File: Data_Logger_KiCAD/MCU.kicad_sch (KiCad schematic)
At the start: 40 parts, among them J1 USB_C_Receptacle_USB2.0_16P, J2 Screw_Terminal_01x02, Q1 Q_NMOS_GSD, SW1 SW_Push, SW2 SW_Push, U2 ESP32-S3, Y2 Crystal, Y3 Crystal_GND24

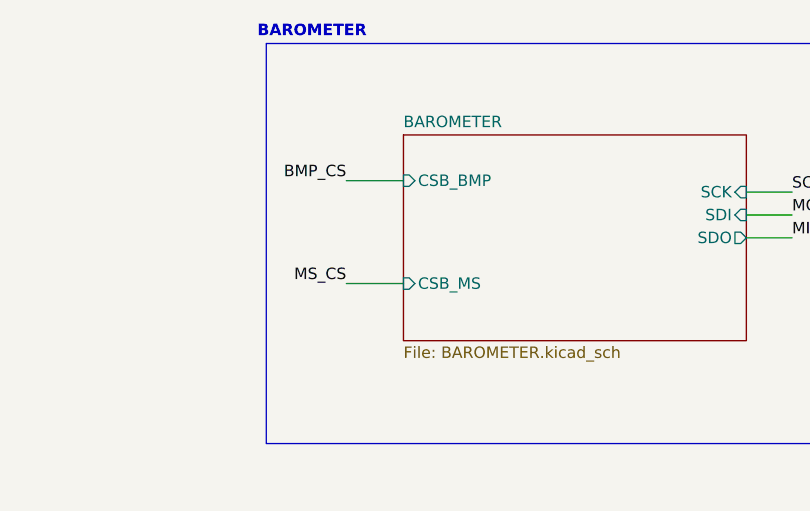
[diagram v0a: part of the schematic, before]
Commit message: synced sheet pins in Data_Logger_Board_pro
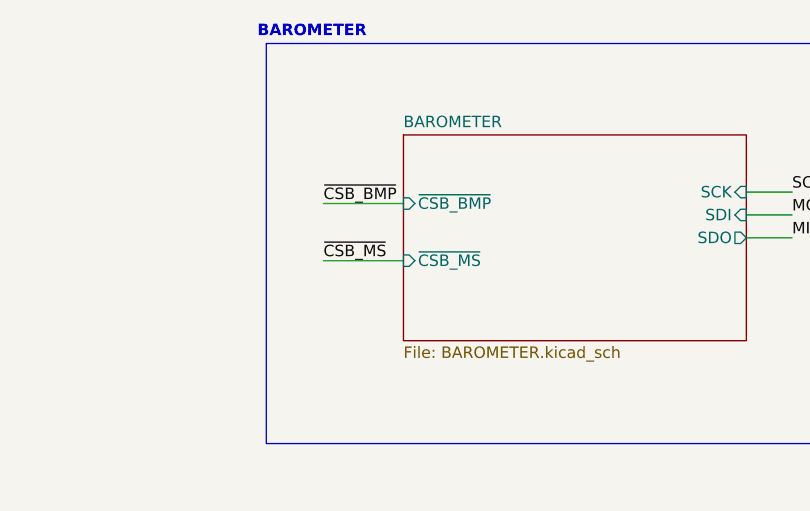
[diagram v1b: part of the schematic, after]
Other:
- sheet BAROMETER ports: added ~{CSB_BMP}, ~{CSB_MS}; removed CSB_BMP, CSB_MS
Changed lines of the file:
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@@
 	(wire
 		(pts
-			(xy 396.24 80.01) (xy 402.59 80.01)
+			(xy 269.24 80.01) (xy 275.59 80.01)
 		)
 		(stroke
@@
 	(wire
 		(pts
-			(xy 269.24 80.01) (xy 275.59 80.01)
+			(xy 185.42 133.35) (xy 193.04 133.35)
 		)
 		(stroke
@@
 	(wire
 		(pts
-			(xy 185.42 133.35) (xy 193.04 133.35)
+			(xy 59.69 87.63) (xy 59.69 85.09)
 		)
 		(stroke
@@
 	(wire
 		(pts
-			(xy 59.69 87.63) (xy 59.69 85.09)
+			(xy 33.02 306.07) (xy 33.02 307.34)
 		)
 		(stroke
@@
 	(wire
 		(pts
-			(xy 33.02 306.07) (xy 33.02 307.34)
+			(xy 185.42 78.74) (xy 195.58 78.74)
 		)
 		(stroke
@@
 	(wire
 		(pts
-			(xy 185.42 78.74) (xy 195.58 78.74)
+			(xy 50.8 306.07) (xy 53.34 306.07)
 		)
 		(stroke
@@
 	(wire
 		(pts
-			(xy 50.8 306.07) (xy 53.34 306.07)
+			(xy 219.71 128.27) (xy 223.52 128.27)
 		)
 		(stroke
@@
 	(wire
 		(pts
-			(xy 219.71 128.27) (xy 223.52 128.27)
+			(xy 393.7 71.12) (xy 402.59 71.12)
 		)
 		(stroke
@@
 	(wire
 		(pts
-			(xy 396.24 68.58) (xy 402.59 68.58)
+			(xy 111.76 135.89) (xy 116.84 135.89)
 		)
 		(stroke
@@
 	(wire
 		(pts
-			(xy 111.76 135.89) (xy 116.84 135.89)
+			(xy 46.99 361.95) (xy 49.53 361.95)
 		)
 		(stroke
@@
 	(wire
 		(pts
-			(xy 46.99 361.95) (xy 49.53 361.95)
+			(xy 215.9 139.7) (xy 215.9 146.05)
 		)
 		(stroke
@@
 	(wire
 		(pts
-			(xy 215.9 139.7) (xy 215.9 146.05)
+			(xy 222.25 74.93) (xy 222.25 77.47)
 		)
 		(stroke
@@
 	(wire
 		(pts
-			(xy 222.25 74.93) (xy 222.25 77.47)
+			(xy 300.99 182.88) (xy 307.34 182.88)
 		)
 		(stroke
@@
 	(wire
 		(pts
-			(xy 300.99 182.88) (xy 307.34 182.88)
+			(xy 55.88 87.63) (xy 59.69 87.63)
 		)
 		(stroke
@@
 	(wire
 		(pts
-			(xy 55.88 87.63) (xy 59.69 87.63)
+			(xy 255.27 177.8) (xy 262.89 177.8)
 		)
 		(stroke
@@
 	(wire
 		(pts
-			(xy 255.27 177.8) (xy 262.89 177.8)
+			(xy 393.7 77.47) (xy 402.59 77.47)
 		)
 		(stroke
@@
 		)
 	)
+	(label "~{CSB_MS}"
+		(at 393.7 77.47 0)
+		(effects
+			(font
+				(size 1.27 1.27)
+			)
+			(justify left bottom)
+		)
+	)
 	(label "MOSI"
 		(at 481.33 74.93 180)
@@
 		)
 	)
-	(label "BMP_CS"
-		(at 396.24 68.58 180)
-		(effects
-			(font
-				(size 1.27 1.27)
-			)
-			(justify right bottom)
-		)
-	)
 	(label "GPS_EXTINT"
 		(at 193.04 110.49 0)
@@
 		)
 	)
-	(label "MS_CS"
-		(at 396.24 80.01 180)
+	(label "MAG_INT"
+		(at 481.33 69.85 180)
 		(effects
 			(font
@@
 		)
 	)
-	(label "MAG_INT"
-		(at 481.33 69.85 180)
+	(label "~{ACCEL_CS}"
+		(at 132.08 125.73 180)
 		(effects
 			(font
@@
 		)
 	)
-	(label "~{ACCEL_CS}"
-		(at 132.08 125.73 180)
+	(label "~{CSB_BMP}"
+		(at 393.7 71.12 0)
 		(effects
 			(font
 				(size 1.27 1.27)
 			)
-			(justify right bottom)
+			(justify left bottom)
 		)
 	)
@@
 			)
 		)
-		(pin "CSB_BMP" input
-			(at 402.59 68.58 180)
+		(pin "SCK" input
+			(at 440.69 69.85 0)
 			(effects
 				(font
 					(size 1.27 1.27)
 				)
-				(justify left)
+				(justify right)
 			)
 		)
-		(pin "CSB_MS" input
-			(at 402.59 80.01 180)
+		(pin "SDI" input
+			(at 440.69 72.39 0)
 			(effects
 				(font
 					(size 1.27 1.27)
 				)
-				(justify left)
+				(justify right)
 			)
 		)
-		(pin "SCK" input
-			(at 440.69 69.85 0)
+		(pin "SDO" output
+			(at 440.69 74.93 0)
 			(effects
 				(font
@@
 			)
 		)
-		(pin "SDI" input
-			(at 440.69 72.39 0)
+		(pin "~{CSB_BMP}" input
+			(at 402.59 71.12 180)
 			(effects
 				(font
 					(size 1.27 1.27)
 				)
-				(justify right)
+				(justify left)
 			)
 		)
-		(pin "SDO" output
-			(at 440.69 74.93 0)
+		(pin "~{CSB_MS}" input
+			(at 402.59 77.47 180)
 			(effects
 				(font
 					(size 1.27 1.27)
 				)
-				(justify right)
+				(justify left)
 			)
 		)

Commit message: update MCU
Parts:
- added D3, D5: D_Schottky, symbol Device:D_Schottky
- added D4: D_Schottky, Diode_SMD:D_SOD-123, symbol Device:D_Schottky
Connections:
- net +BATT: now also D5.2 (A)
- net IMU_CS: no longer U2.9 (GPIO4)
- net MAG_INT: now also U2.11 (GPIO6); no longer U2.10 (GPIO5)
- net VBUS: now also D3.2 (A)
- net BMP_CS renamed ~{BMP_CS}
- net MAG_CS renamed ~{MAG_CS}
- net MS_CS renamed ~{MS_CS}
- new net PWR_IN: D3.1 (K), D5.1 (K)
- new net ~{IMU_CS}: U2.9 (GPIO4)
- new net ~{RADIO_CS}: U2.10 (GPIO5)
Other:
- sheet PWR ports: added PWR_IN, PWR_OUT; removed none
- note added: "Reverse-Polarity Protection"

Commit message: diode part#
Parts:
- D3, D5: footprint (none) -> Diode_SMD:D_SOD-123; LCSC (none) -> C8598
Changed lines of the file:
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@@
 		)
 	)
+	(label "PWR_IN"
+		(at 397.51 135.89 180)
+		(effects
+			(font
+				(size 1.27 1.27)
+			)
+			(justify right bottom)
+		)
+	)
 	(label "~{CSB_MS}"
 		(at 393.7 77.47 0)
@@
 		)
 	)
+	(label "PWR_OUT"
+		(at 441.96 135.89 0)
+		(effects
+			(font
+				(size 1.27 1.27)
+			)
+			(justify left bottom)
+		)
+	)
 	(label "BATTERY_SENSE"
 		(at 132.08 115.57 180)
@@
 			)
 		)
-		(property "Footprint" ""
+		(property "Footprint" "Diode_SMD:D_SOD-123"
 			(at 162.56 278.13 0)
 			(effects
@@
 			)
 		)
+		(property "LCSC" "C8598"
+			(at 162.56 278.13 0)
+			(effects
+				(font
+					(size 1.27 1.27)
+				)
+				(hide yes)
+			)
+		)
 		(pin "1"
 		)
@@
 			)
 		)
-		(property "Footprint" ""
+		(property "Footprint" "Diode_SMD:D_SOD-123"
 			(at 147.32 278.13 0)
 			(effects
@@
 			(at 147.32 278.13 0)
 			(effects
+				(font
+					(size 1.27 1.27)
+				)
+				(hide yes)
+			)
+		)
+		(property "LCSC" "C8598"
+			(at 147.32 278.13 0)
+			(effects

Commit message: rem old files and add LCSC #'s
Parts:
- removed D4: D_Schottky, Diode_SMD:D_SOD-123, symbol Device:D_Schottky
- AE1: footprint (none) -> RF_Antenna:Molex_47948-0001_2.4Ghz; LCSC (none) -> C152351
- C3: LCSC C96446 -> C19702
- R13: value 10 -> 100; LCSC C25077 -> C25076
- U2: LCSC (none) -> C2913192
- Y2: footprint (none) -> Crystal:Crystal_SMD_3215-2Pin_3.2x1.5mm; LCSC (none) -> C32346
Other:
- removed sheet RF_WIFI
- sheet BAROMETER ports: added ~{BMP_CS}, ~{MS_CS}; removed ~{CSB_BMP}, ~{CSB_MS}
- note added: "Buzzer"
- note added: "Reverse-Polarity Protection + Power"
- note removed: "POWER"
- note removed: "RF WIFI ANTENNA"
- note removed: "Reverse-Polarity Protection"

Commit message: partial MCU layout
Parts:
- BZ1: footprint (none) -> Buzzer_Beeper:Buzzer_Murata_PKMCS0909E
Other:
- note added: "Correct buzzer footprint if needed"
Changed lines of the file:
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@@
 		)
 	)
+	(text "Correct buzzer footprint if needed"
+		(exclude_from_sim no)
+		(at 58.928 338.582 0)
+		(effects
+			(font
+				(size 1.27 1.27)
+			)
+		)
+	)
 	(text "Buzzer"
 		(exclude_from_sim no)
@@
 			)
 		)
-		(property "Footprint" ""
+		(property "Footprint" "Buzzer_Beeper:Buzzer_Murata_PKMCS0909E"
 			(at 59.055 349.25 90)
 			(effects

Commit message: more progress on MCU layout
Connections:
- net +3V3: now also C10.1, U2.46 (VDD3P3_CPU)
- net MAG_INT: now also U2.48 (MTMS); no longer U2.11 (GPIO6)
- net flash/VDD: now also U2.29 (VDD_SPI); no longer U2.46 (VDD3P3_CPU)
- net ~{IMU_CS}: now also U2.11 (GPIO6); no longer U2.9 (GPIO4)
- net ~{MAG_CS}: now also U2.9 (GPIO4); no longer U2.8 (GPIO3)
- net ~{RADIO_CS}: now also U2.12 (GPIO7); no longer U2.10 (GPIO5)
- net ANT_SW: now reaches U2.43 (GPIO38)
- net RADIO_INT: now reaches U2.45 (MTDO)
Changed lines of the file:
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@@
 	)
 	(junction
+		(at 222.25 74.93)
+		(diameter 0)
+		(color 0 0 0 0)
+	)
+	(junction
 		(at 57.15 354.33)
 		(diameter 0)
@@
 	(wire
 		(pts
-			(xy 167.64 85.09) (xy 167.64 78.74)
-		)
-		(stroke
-			(width 0)
-			(type default)
-		)
-	)
-	(wire
-		(pts
 			(xy 147.32 237.49) (xy 153.67 237.49)
 		)
@@
 	(wire
 		(pts
-			(xy 165.1 85.09) (xy 165.1 74.93)
-		)
-		(stroke
-			(width 0)
-			(type default)
-		)
-	)
-	(wire
-		(pts
 			(xy 195.58 78.74) (xy 195.58 80.01)
 		)
@@
 	(wire
 		(pts
-			(xy 167.64 78.74) (xy 185.42 78.74)
-		)
-		(stroke
-			(width 0)
-			(type default)
-		)
-	)
-	(wire
-		(pts
 			(xy 269.24 80.01) (xy 275.59 80.01)
 		)
@@
 	(wire
 		(pts
+			(xy 165.1 78.74) (xy 185.42 78.74)
+		)
+		(stroke
+			(width 0)
+			(type default)
+		)
+	)
+	(wire
+		(pts
 			(xy 166.37 63.5) (xy 166.37 64.77)
 		)
@@
 	(wire
 		(pts
+			(xy 167.64 74.93) (xy 167.64 85.09)
+		)
+		(stroke
+			(width 0)
+			(type default)
+		)
+	)
+	(wire
+		(pts
 			(xy 132.08 107.95) (xy 139.7 107.95)
 		)
@@
 	(wire
 		(pts
+			(xy 222.25 72.39) (xy 222.25 74.93)
+		)
+		(stroke
+			(width 0)
+			(type default)
+		)
+	)
+	(wire
+		(pts
 			(xy 185.42 143.51) (xy 193.04 143.51)
 		)
@@
 	(wire
 		(pts
-			(xy 165.1 74.93) (xy 222.25 74.93)
+			(xy 55.88 80.01) (xy 59.69 80.01)
 		)
 		(stroke
@@
 	(wire
 		(pts
-			(xy 55.88 80.01) (xy 59.69 80.01)
+			(xy 132.08 148.59) (xy 139.7 148.59)
 		)
 		(stroke
@@
 	(wire
 		(pts
-			(xy 132.08 148.59) (xy 139.7 148.59)
+			(xy 38.1 205.74) (xy 38.1 204.47)
 		)
 		(stroke
@@
 	(wire
 		(pts
-			(xy 38.1 205.74) (xy 38.1 204.47)
+			(xy 154.94 278.13) (xy 154.94 287.02)
 		)
 		(stroke
@@
 	(wire
 		(pts
-			(xy 154.94 278.13) (xy 154.94 287.02)
+			(xy 60.96 62.23) (xy 60.96 67.31)
 		)
 		(stroke
@@
 	(wire
 		(pts
-			(xy 60.96 62.23) (xy 60.96 67.31)
+			(xy 45.72 297.18) (xy 54.61 297.18)
 		)
 		(stroke
@@
 	(wire
 		(pts
-			(xy 45.72 297.18) (xy 54.61 297.18)
+			(xy 100.33 63.5) (xy 100.33 64.77)
 		)
 		(stroke
@@
 	(wire
 		(pts
-			(xy 100.33 63.5) (xy 100.33 64.77)
+			(xy 165.1 78.74) (xy 165.1 85.09)
 		)
 		(stroke
@@
 	(wire
 		(pts
+			(xy 167.64 74.93) (xy 222.25 74.93)
+		)
+		(stroke
+			(width 0)
+			(type default)
+		)
+	)
+	(wire
+		(pts
 			(xy 185.42 113.03) (xy 193.04 113.03)
 		)
@@
 		)
 	)
+	(label "MAG_INT"
+		(at 193.04 138.43 0)
+		(effects
+			(font
+				(size 1.27 1.27)
+			)
+			(justify left bottom)
+		)
+	)
 	(label "MISO"
 		(at 425.45 74.93 0)
@@
 		)
 	)
-	(label "MAG_INT"
-		(at 132.08 107.95 180)
-		(effects
-			(font
-				(size 1.27 1.27)
-			)
-			(justify right bottom)
-		)
-	)
 	(label "TIMEPULSE"
 		(at 193.04 113.03 0)
@@
 		)
 	)
+	(label "ANT_SW"
+		(at 193.04 128.27 0)
+		(effects
+			(font
+				(size 1.27 1.27)
+			)
+			(justify left bottom)
+		)
+	)
 	(label "PWR_IN"
 		(at 138.43 300.99 180)
@@
 		)
 	)
+	(label "RADIO_INT"
+		(at 193.04 133.35 0)
+		(effects
+			(font
+				(size 1.27 1.27)
+			)
+			(justify left bottom)
+		)
+	)
 	(label "~{MS_CS}"
 		(at 373.38 77.47 0)
@@
 		)
 	)
-	(label "~{IMU_CS}"
-		(at 132.08 102.87 180)
+	(label "ANT_SW"
+		(at 269.24 74.93 180)
 		(effects
 			(font
@@
 		)
 	)
-	(label "~{RADIO_CS}"
-		(at 132.08 105.41 180)
+	(label "ACCEL_INT"
+		(at 147.32 240.03 180)
 		(effects
 			(font
@@
 		)
 	)
-	(label "ACCEL_INT"
-		(at 147.32 240.03 180)
+	(label "XTAL_P"
+		(at 132.08 151.13 180)
 		(effects
 			(font
@@
 		)
 	)
-	(label "XTAL_P"
-		(at 132.08 151.13 180)
+	(label "~{ACCEL_CS}"
+		(at 147.32 232.41 180)
 		(effects
 			(font
@@
 		)
 	)
-	(label "~{ACCEL_CS}"
-		(at 147.32 232.41 180)
+	(label "RADIO_INT"
+		(at 269.24 80.01 180)
 		(effects
 			(font
@@
 		)
 	)
+	(label "~{RADIO_CS}"
+		(at 132.08 110.49 180)
+		(effects
+			(font
+				(size 1.27 1.27)
+			)
+			(justify right bottom)
+		)
+	)
 	(label "~{RADIO_RESET}"
 		(at 269.24 87.63 180)
@@
 		)
 	)
+	(label "~{IMU_CS}"
+		(at 132.08 107.95 180)
+		(effects
+			(font
+				(size 1.27 1.27)
+			)
+			(justify right bottom)
+		)
+	)
 	(label "~{RADIO_RESET}"
 		(at 193.04 118.11 0)
@@
 		)
 	)
-	(label "~{MAG_CS}"
-		(at 132.08 100.33 180)
-		(effects
-			(font
-				(size 1.27 1.27)
-			)
-			(justify right bottom)
-		)
-	)
 	(label "XTAL_P"
 		(at 68.58 297.18 0)
@@
 		)
 	)
+	(label "~{MAG_CS}"
+		(at 132.08 102.87 180)
+		(effects
+			(font
+				(size 1.27 1.27)
+			)
+			(justify right bottom)
+		)
+	)
 	(netclass_flag ""
 		(length 2.54)
@@
 					(unit 1)
 				)
+			)
+		)
+	)
+	(symbol
+		(lib_id "power:+3V3")
+		(at 222.25 72.39 0)
+		(unit 1)
+		(exclude_from_sim no)
+		(in_bom yes)
+		(on_board yes)
+		(dnp no)
+		(fields_autoplaced yes)
+		(property "Reference" "#PWR053"
+			(at 222.25 76.2 0)
+			(effects
+				(font
+					(size 1.27 1.27)
+				)
+				(hide yes)
+			)
+		)
+		(property "Value" "+3V3"
+			(at 222.25 67.31 0)
+			(effects
+				(font
+					(size 1.27 1.27)
+				)
+			)
+		)
+		(property "Footprint" ""
+			(at 222.25 72.39 0)
+			(effects
+				(font
+					(size 1.27 1.27)
+				)
+				(hide yes)
+			)
+		)
+		(property "Datasheet" ""
+			(at 222.25 72.39 0)
+			(effects
+				(font
+					(size 1.27 1.27)
+				)
+				(hide yes)
+			)
+		)
+		(property "Description" "Power symbol creates a global label with name \"+3V3\""
+			(at 222.25 72.39 0)
+			(effects
+				(font
+					(size 1.27 1.27)
+				)
+				(hide yes)
+			)
+		)
+		(pin "1"
+		)
+		(instances
+			(project ""
+				(path "/db968e42-3ace-4cc9-9096-9d8f48135c40/795ab2be-9db7-4254-b05c-ac2b60177344"
+					(reference "#PWR053")
+					(unit 1)
+				)

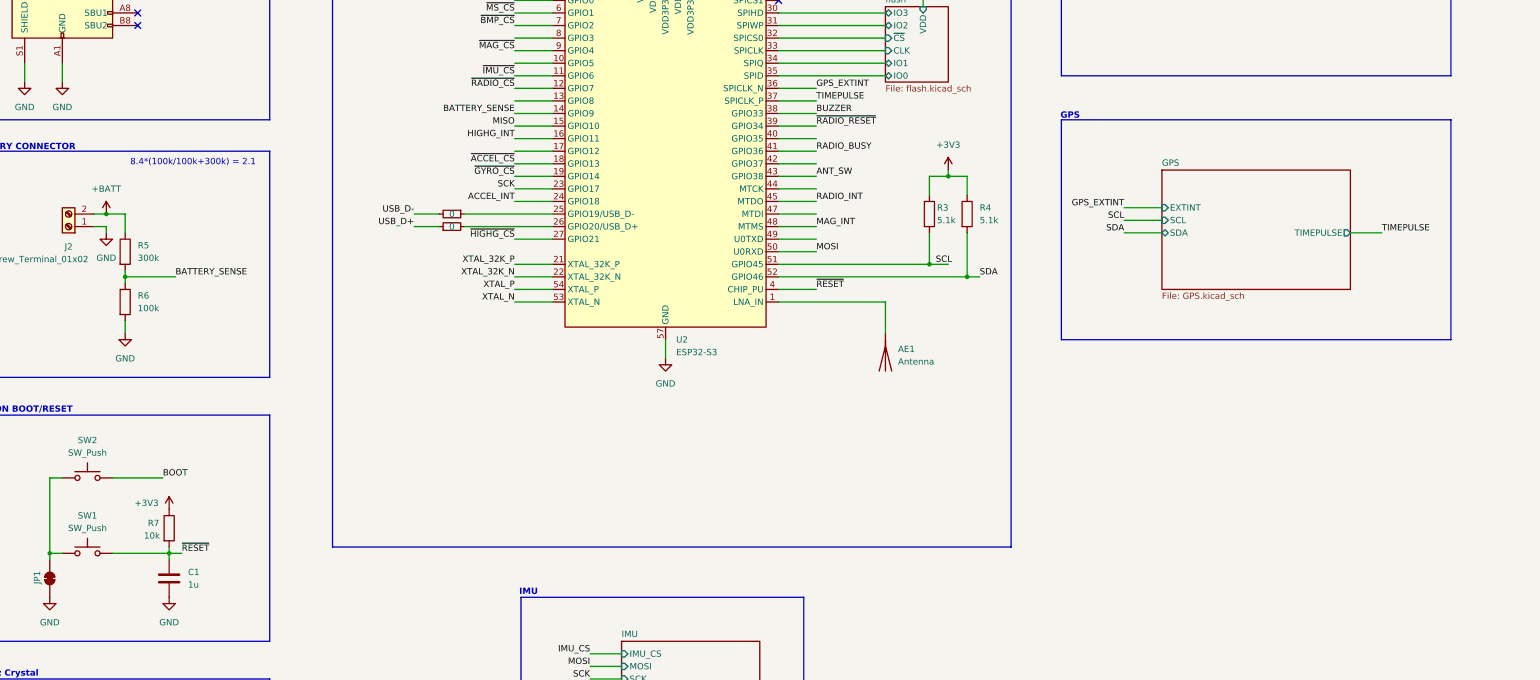
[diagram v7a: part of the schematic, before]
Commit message: add microSD
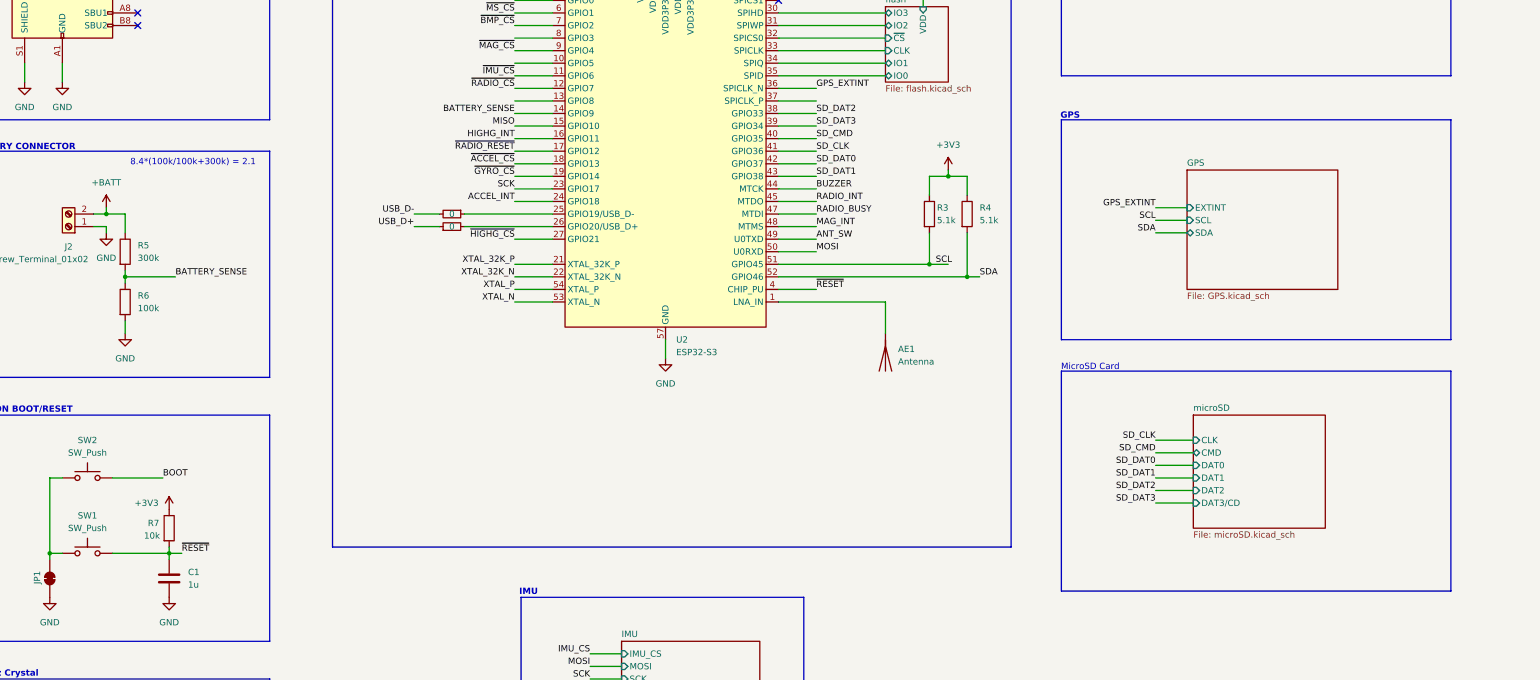
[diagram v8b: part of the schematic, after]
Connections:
- net ANT_SW: now also U2.49 (U0TXD); no longer U2.43 (GPIO38)
- net BUZZER: now also U2.44 (MTCK); no longer U2.38 (GPIO33)
- net RADIO_BUSY: now also U2.47 (MTDI); no longer U2.41 (GPIO36)
- net ~{RADIO_RESET}: now also U2.17 (GPIO12); no longer U2.39 (GPIO34)
- net SD_CMD: now reaches U2.40 (GPIO35)
- net SD_DAT0: now reaches U2.42 (GPIO37)
- net TIMEPULSE: no longer names the net of U2.37 (SPICLK_P)
- new net SD_CLK: U2.41 (GPIO36)
- new net SD_DAT1: U2.43 (GPIO38)
- new net SD_DAT2: U2.38 (GPIO33)
- new net SD_DAT3: U2.39 (GPIO34)
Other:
- added sheet microSD (microSD.kicad_sch)
- sheet GPS ports: added none; removed TIMEPULSE
- note added: "MicroSD Card"
